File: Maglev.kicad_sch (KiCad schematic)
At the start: 39 parts, among them J1 629722000214, J2 691103110002, J3 61300621121, U1 WE-TVS-82400102, U2 ESP32-S3-WROOM-1

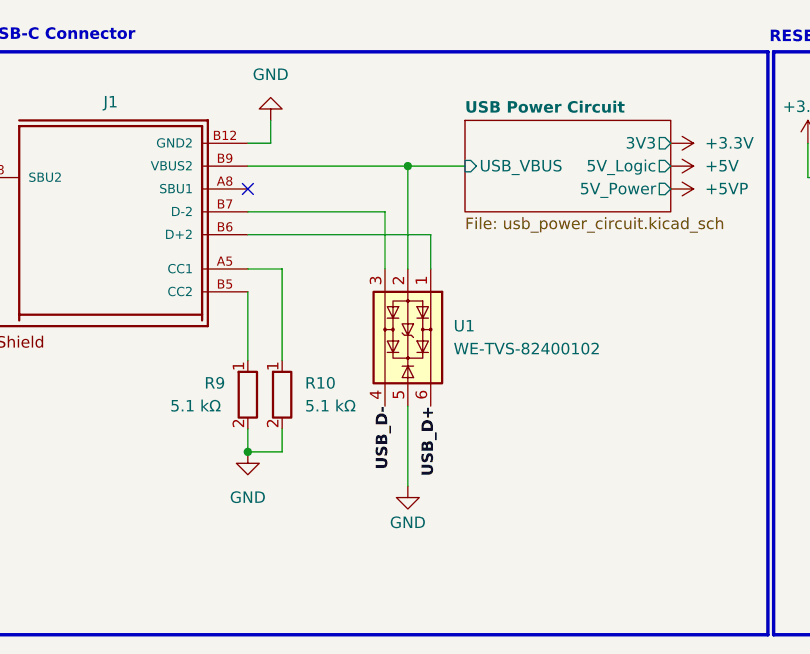
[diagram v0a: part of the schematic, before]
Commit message: minor changes an corrected tvs diode
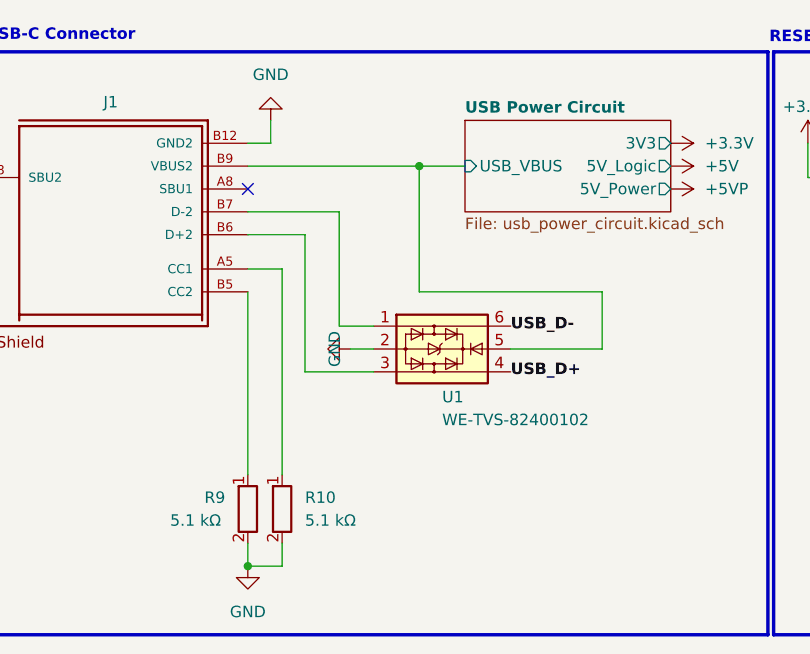
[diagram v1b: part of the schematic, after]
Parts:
- TP1, TP2, TP3, TP4: now left out of the parts list
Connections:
- net GND: now also U1.2; no longer U1.5
- net USB Power Circuit/USB_VBUS: now also U1.5; no longer U1.2
- net USB_D+: now also U1.4; no longer U1.6
- net USB_D-: now also U1.6; no longer U1.4
- net at J1.A6 (D+1), J1.B6 (D+2): now also U1.3; no longer U1.1
- net at J1.A7 (D-1), J1.B7 (D-2): now also U1.1; no longer U1.3
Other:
- moved on the sheet: R10, R9, U1

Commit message: eFuse Fehler angepasst plus allgemeine Änderungen / BOM aktualisiert
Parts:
- U2: Manufacturer (none) -> Esspresif; Part Number (none) -> ESP32S3WM1UN16R8
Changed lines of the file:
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@@
+			)
+		)
+		(property "Manufacturer" "Esspresif"
+			(at 96.52 74.93 0)
+			(hide yes)
+			(show_name no)
+			(do_not_autoplace no)
+			(effects
+				(font
+					(size 1.27 1.27)
+				)
+			)
+		)
+		(property "Part Number" "ESP32S3WM1UN16R8"
+			(at 96.52 74.93 0)
+			(hide yes)
+			(show_name no)
+			(do_not_autoplace no)
+			(effects
+				(font
+					(size 1.27 1.27)
+				)
 			)
 		)
